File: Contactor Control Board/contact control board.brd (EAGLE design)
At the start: 63.2 x 38.1 mm, 23 parts, among them Q4 MOSFET-NCHANNELFQP30N06L

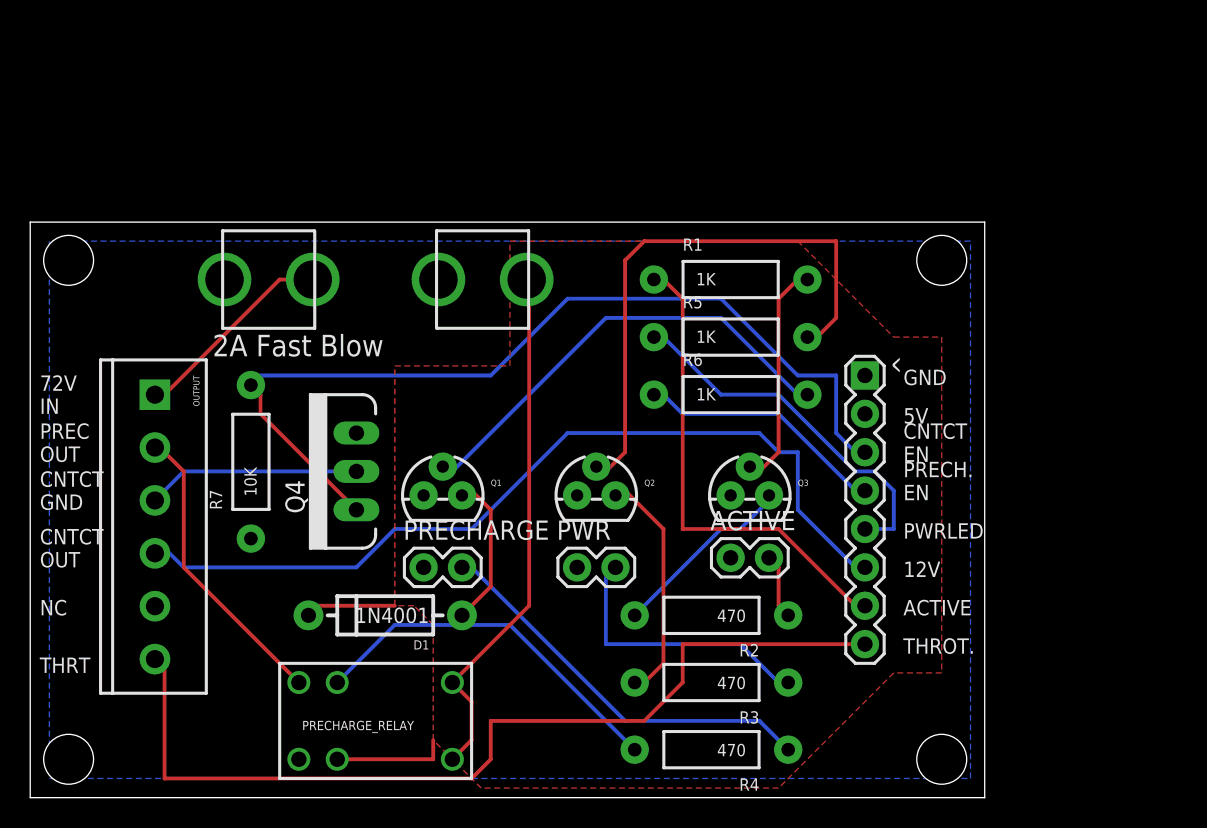
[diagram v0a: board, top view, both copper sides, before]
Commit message: Adding capacitor charge state sense for CCB
Theoretical part selection. Not for usage until testing!
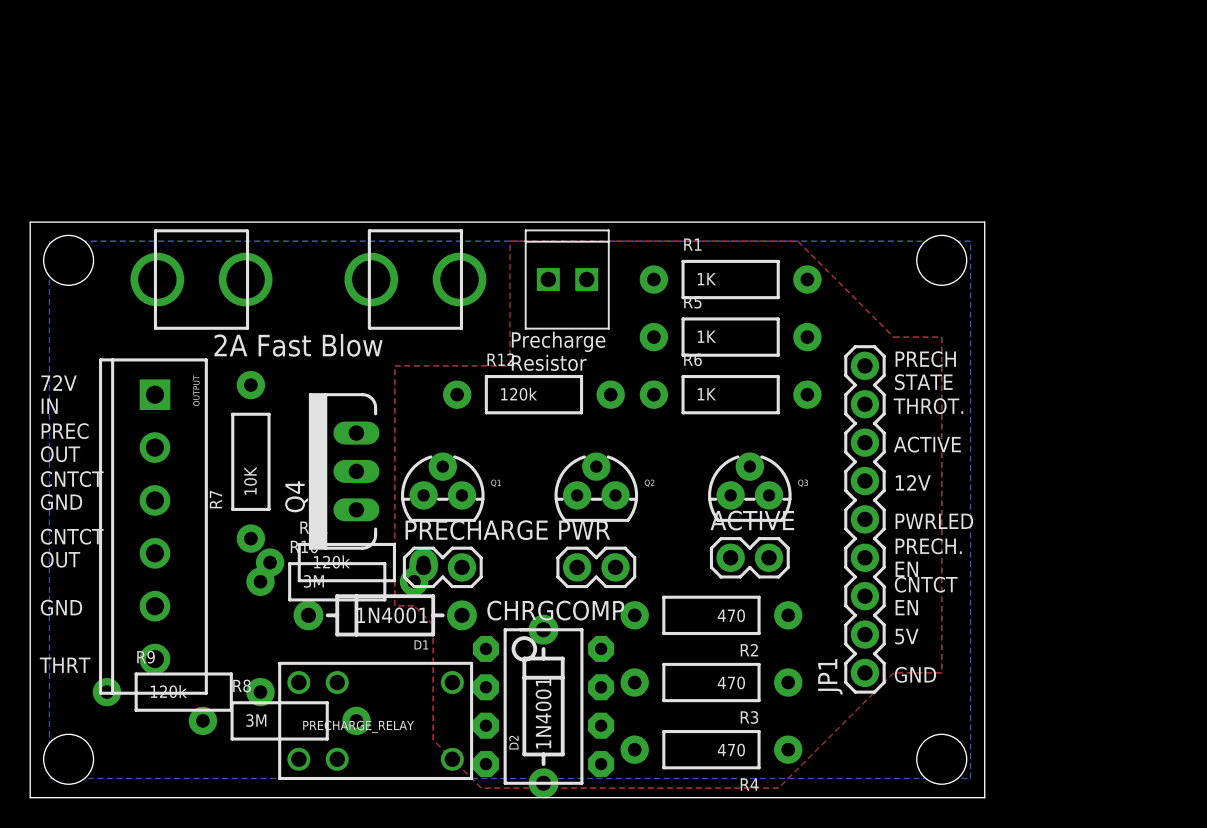
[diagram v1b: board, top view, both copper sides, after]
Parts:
- removed ^: 8pin, SparkFun-Connectors:1X08
- added CHRGCOMP: LM358, SparkFun-AnalogIC:DIP08
- added D2: 1N4001, SparkFun-DiscreteSemi:DIODE-1N4001
- added JP1: M09, SparkFun-Connectors:1X09
- added R10, R8: 3M, SparkFun-Resistors:AXIAL-0.4
- added R11, R12, R9: 120k, SparkFun-Resistors:AXIAL-0.4
- added RESISTOR: M022.54MM_SCREWTERM, SparkFun-Connectors:1X02_2.54_SCREWTERM
- moved PRECHARGE_FUSE 4.45 mm to (18.4, 34.3)
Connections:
- new net CAP_CHARGE_REF: CHRGCOMP.2, R11.P$2, R12.P$1
- new net CAP_CHARGE_V_CURR: CHRGCOMP.3, R8.P$2, R9.P$1
- new net N$3: R10.P$2, R11.P$1
- new net N$5: CHRGCOMP.1, D2.A
- new net PRECHARGE_INPUT: PRECHARGE_RELAY.5, PRECHARGE_RELAY.6, R9.P$2, RESISTOR.P2
- new net PRECH_STATE: D2.C, JP1.9
- net 12V: now also JP1.6; no longer ^.6
- net 5V: now also CHRGCOMP.8, JP1.2; no longer ^.2
- net 72V_IN_FUSED: now also R10.P$1, R8.P$1, RESISTOR.P1; no longer PRECHARGE_RELAY.5, PRECHARGE_RELAY.6
- net ACTIVE_LED_EN: now also JP1.7; no longer ^.7
- net CONTACT_EN: now also JP1.3; no longer ^.3
- net GND: now also CHRGCOMP.4, JP1.1, OUTPUT.5, R12.P$2; no longer ^.1
- net PRECHARGE_EN: now also JP1.4; no longer ^.4
- net PWR_LED: now also JP1.5; no longer ^.5
- net THROTTLE: now also JP1.8; no longer ^.8
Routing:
- net THROTTLE: track 61.3 -> 0.00 mm
- net CONTACT_EN: track 60.6 -> 0.00 mm
- net 12V: track 57.2 -> 0.00 mm
- net PWR_TRAN_IN: track 37.2 -> 0.00 mm
- net PRECH_TRAN_COLLECTOR: track 35.5 -> 0.00 mm
- net 72V_IN_FUSED: track 35.1 -> 0.00 mm
- net ACTIVE_LED_EN: track 31.8 -> 0.00 mm
- net PRECH_TRAN_IN: track 30.5 -> 0.00 mm
- net N$14: track 26.6 -> 0.00 mm
- net PWR_LED: track 24.5 -> 0.00 mm
- net PRECHARGE_OUT: track 19.6 -> 0.00 mm
- net N$12: track 18.8 -> 0.00 mm
- net PRECHARGE_EN: track 16.6 -> 0.00 mm
- net N$2: track 15.6 -> 0.00 mm
- net ACTIVE_TRAN_IN: track 15.1 -> 0.00 mm
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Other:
- board text added: "PRECH STATE"
- board text added: "Precharge Resistor"
- board text removed: "NC"

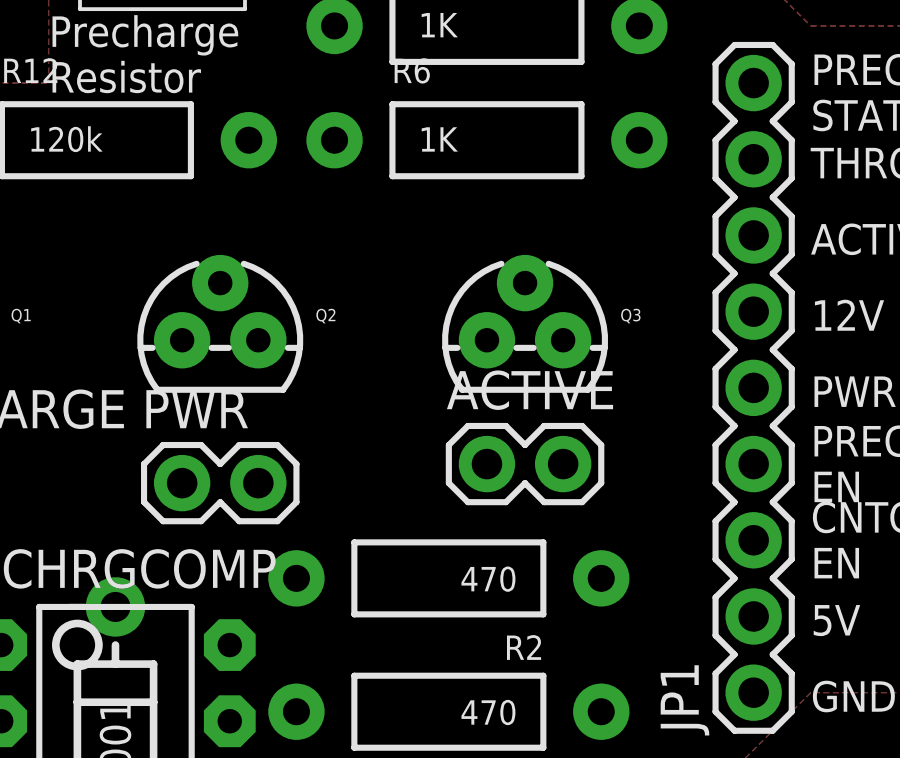
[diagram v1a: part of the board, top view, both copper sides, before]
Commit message: Added inverter w/ schmitt trigger to the output of the opamp to fixup its outputs.
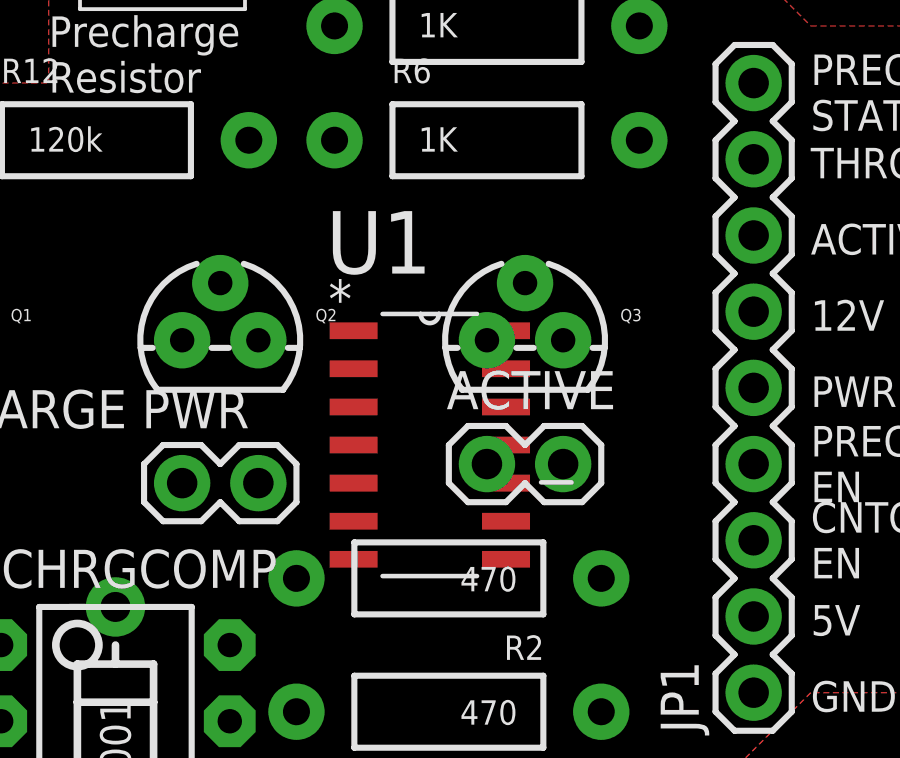
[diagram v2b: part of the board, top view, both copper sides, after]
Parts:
- added U1: 74ACT14SC, Fairchild_By_element14_Batch_1:SOIC127P600X175-14N
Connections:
- new net N$6: U1.1
- net 5V: now also U1.14
- net GND: now also U1.7
- net PRECH_STATE: now also U1.2; no longer D2.C
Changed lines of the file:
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@@
 <layer number="23" name="tOrigins" color="15" fill="1" visible="yes" active="yes"/>
 <layer number="24" name="bOrigins" color="15" fill="1" visible="yes" active="yes"/>
-<layer number="25" name="tNames" color="16" fill="1" visible="yes" active="yes"/>
+<layer number="25" name="tNames" color="16" fill="1" visible="no" active="yes"/>
 <layer number="26" name="bNames" color="16" fill="1" visible="no" active="yes"/>
 <layer number="27" name="tValues" color="7" fill="1" visible="no" active="yes"/>
@@
 <element name="R11" library="SparkFun-Resistors" package="AXIAL-0.4" value="120k" x="20.955" y="15.5575"/>
 <element name="R12" library="SparkFun-Resistors" package="AXIAL-0.4" value="120k" x="33.3375" y="26.67"/>
+<element name="U1" library="Fairchild_By_element14_Batch_1" package="SOIC127P600X175-14N" value="74ACT14SC" x="44.45" y="16.51">
+<attribute name="PACKAGE" value="SOIC-14" x="44.45" y="16.51" size="1.778" layer="27" font="vector" ratio="15" display="off"/>
+<attribute name="OC_NEWARK" value="78K6179" x="44.45" y="16.51" size="1.778" layer="27" font="vector" ratio="15" display="off"/>
+<attribute name="MPN" value="74ACT14SC" x="44.45" y="16.51" size="1.778" layer="27" font="vector" ratio="15" display="off"/>
+<attribute name="SUPPLIER" value="Fairchild" x="44.45" y="16.51" size="1.778" layer="27" font="vector" ratio="15" display="off"/>
+<attribute name="OC_FARNELL" value="3734936" x="44.45" y="16.51" size="1.778" layer="27" font="vector" ratio="15" display="off"/>
+</element>
 </elements>
 <signals>
@@
 <contactref element="JP1" pad="2"/>
 <contactref element="CHRGCOMP" pad="8"/>
-<wire x1="26.035" y1="15.24" x2="18.415" y2="12.065" width="0" layer="19" extent="1-1"/>
+<contactref element="U1" pad="14"/>
+<wire x1="46.355" y1="15.875" x2="55.245" y2="10.795" width="0" layer="19" extent="1-1"/>
+<wire x1="36.195" y1="15.24" x2="46.355" y2="15.875" width="0" layer="19" extent="1-1"/>
+<wire x1="37.7825" y1="9.8425" x2="36.195" y2="15.24" width="0" layer="19" extent="1-1"/>
+<wire x1="26.035" y1="15.24" x2="36.195" y2="15.24" width="0" layer="19" extent="1-1"/>
+<wire x1="18.415" y1="12.065" x2="26.035" y2="15.24" width="0" layer="19" extent="1-1"/>
 <wire x1="20.32" y1="2.54" x2="18.415" y2="12.065" width="0" layer="19" extent="1-1"/>
+<wire x1="46.99" y1="20.32" x2="18.415" y2="12.065" width="0" layer="19" extent="1-1"/>
 </signal>
 <signal name="GND">
@@
 <contactref element="OUTPUT" pad="5"/>
 <contactref element="R12" pad="P$2"/>
-<wire x1="8.255" y1="12.67" x2="38.4175" y2="26.67" width="0" layer="19" extent="1-1"/>
+<contactref element="U1" pad="7"/>
+<wire x1="36.195" y1="20.0025" x2="46.355" y2="20.0025" width="0" layer="19" extent="1-1"/>
+<wire x1="38.4175" y1="26.67" x2="36.195" y2="20.0025" width="0" layer="19" extent="1-1"/>
+<wire x1="26.035" y1="20.0025" x2="36.195" y2="20.0025" width="0" layer="19" extent="1-1"/>
+<wire x1="21.59" y1="24.13" x2="26.035" y2="20.0025" width="0" layer="19" extent="1-1"/>
+<wire x1="14.605" y1="17.145" x2="21.59" y2="24.13" width="0" layer="19" extent="1-1"/>
+<wire x1="8.255" y1="12.67" x2="14.605" y2="17.145" width="0" layer="19" extent="1-1"/>
+<wire x1="55.245" y1="8.255" x2="46.355" y2="20.0025" width="0" layer="19" extent="1-1"/>
+<wire x1="30.1625" y1="2.2225" x2="26.035" y2="20.0025" width="0" layer="19" extent="1-1"/>
+<wire x1="41.91" y1="12.7" x2="8.255" y2="12.67" width="0" layer="19" extent="1-1"/>
 </signal>
 <signal name="CONTACT_EN">
@@
 <signal name="PRECH_STATE">
 <contactref element="JP1" pad="9"/>
-<contactref element="D2" pad="C"/>
-<wire x1="33.9725" y1="11.1125" x2="55.245" y2="28.575" width="0" layer="19" extent="1-1"/>
+<contactref element="U1" pad="2"/>
+<wire x1="41.91" y1="19.05" x2="55.245" y2="28.575" width="0" layer="19" extent="1-1"/>
 </signal>
 <signal name="PRECHARGE_INPUT">
@@
 <wire x1="5.08" y1="6.985" x2="21.59" y2="5.08" width="0" layer="19" extent="1-1"/>
 </signal>
+<signal name="N$6">
+<contactref element="U1" pad="1"/>
+</signal>
 </signals>
